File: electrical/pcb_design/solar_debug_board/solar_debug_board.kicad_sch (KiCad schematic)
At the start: 1 part

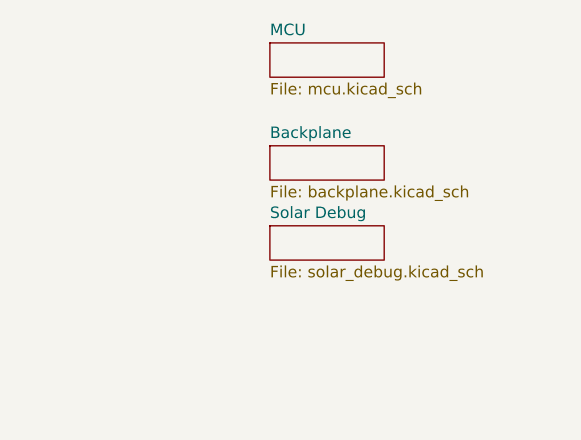
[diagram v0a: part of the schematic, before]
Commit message: Fixed bug in debug header; it was oriented incorrectly. Tweaked schematic layout and part properties. Added production files.
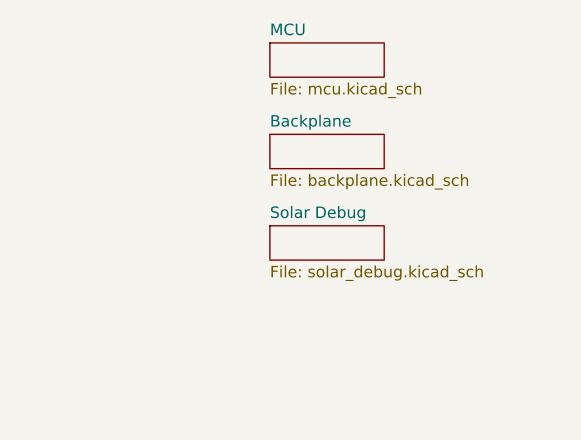
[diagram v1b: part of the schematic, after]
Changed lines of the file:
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@@
     (pin "1")
     (instances
-      (project "debug_core_board"
+      (project "solar_debug_board"
         (path "/476cf7fd-4f82-4468-99c1-e027b17f5088"
           (reference "#PWR03") (unit 1)
@@
     (pin "1")
     (instances
-      (project "debug_core_board"
+      (project "solar_debug_board"
         (path "/476cf7fd-4f82-4468-99c1-e027b17f5088"
           (reference "#PWR01") (unit 1)
@@
     (pin "17")
     (instances
-      (project "debug_core_board"
+      (project "solar_debug_board"
         (path "/476cf7fd-4f82-4468-99c1-e027b17f5088"
           (reference "PCB1") (unit 1)
@@
     )
   )
-  (sheet (at 226.06 36.83) (size 12.7 3.81) (fields_autoplaced)
+  (sheet (at 226.06 35.56) (size 12.7 3.81) (fields_autoplaced)
     (stroke (width 0.1524) (type solid))
     (fill (color 0 0 0 0.0000))
-    (property "Sheetname" "Backplane" (at 226.06 36.1184 0)
+    (property "Sheetname" "Backplane" (at 226.06 34.8484 0)
       (effects (font (size 1.27 1.27)) (justify left bottom))
     )
-    (property "Sheetfile" "backplane.kicad_sch" (at 226.06 41.2246 0)
+    (property "Sheetfile" "backplane.kicad_sch" (at 226.06 39.9546 0)
       (effects (font (size 1.27 1.27)) (justify left top))
     )
     (instances
-      (project "debug_core_board"
+      (project "solar_debug_board"
         (path "/476cf7fd-4f82-4468-99c1-e027b17f5088" (page "3"))
       )
@@
     )
     (instances
-      (project "debug_core_board"
+      (project "solar_debug_board"
         (path "/476cf7fd-4f82-4468-99c1-e027b17f5088" (page "2"))
       )
@@
     )
     (instances
-      (project "debug_core_board"
+      (project "solar_debug_board"
         (path "/476cf7fd-4f82-4468-99c1-e027b17f5088" (page "4"))
       )
